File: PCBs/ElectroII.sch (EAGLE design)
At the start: 13 parts, among them U1 RFM95W-868S2

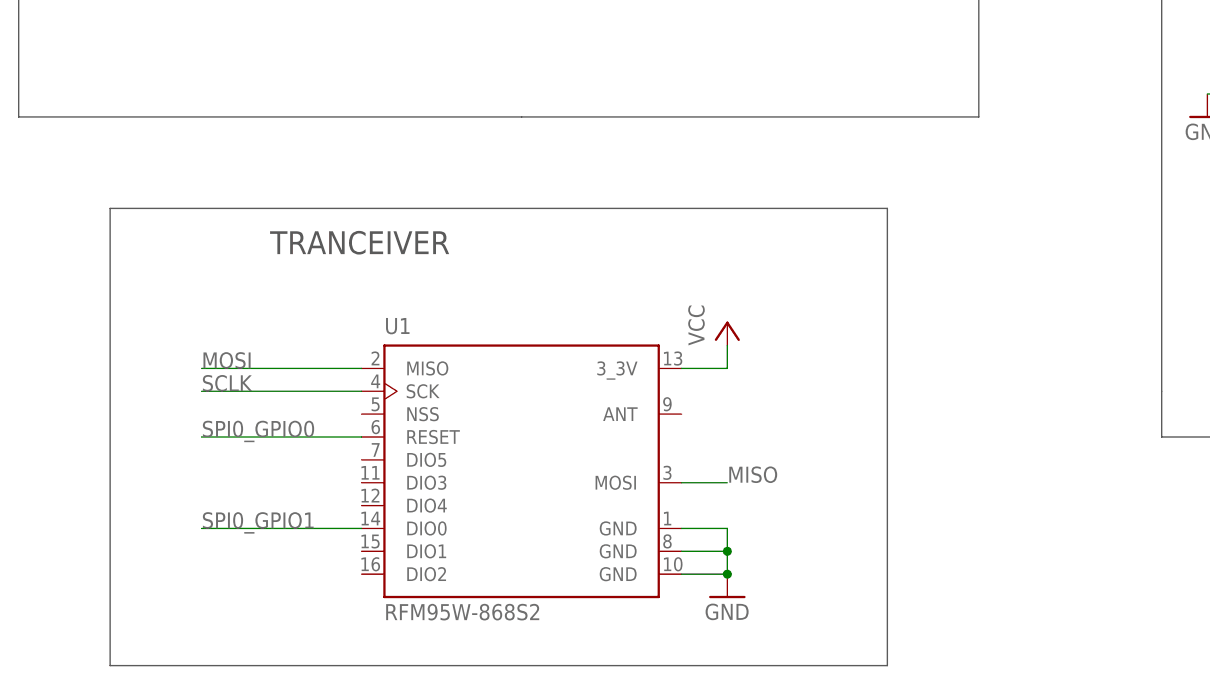
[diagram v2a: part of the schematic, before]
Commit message: Laid out rough PCB for Electro II
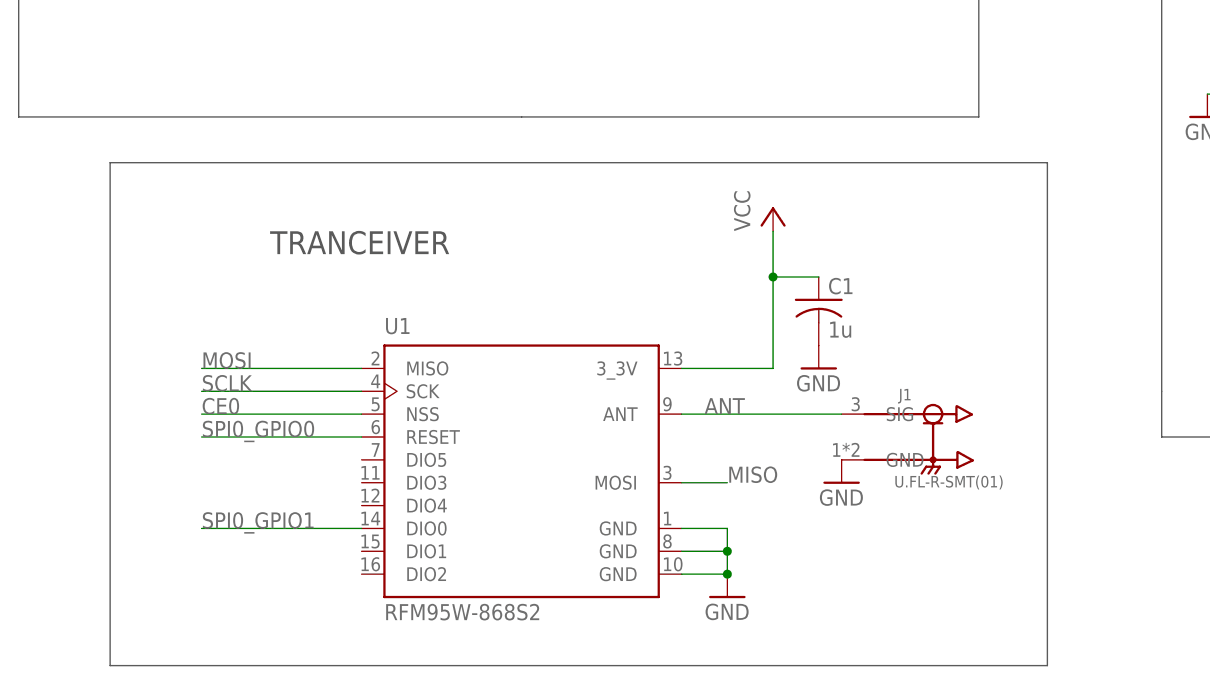
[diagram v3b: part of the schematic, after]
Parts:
- added C1: 1u, RTR Main Library:C-ALL_PACKAGESC1206
- added J1: U.FL-R-SMT(01), RTR Main Library:U.FL-R-SMT(01)
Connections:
- new net ANT: J1.SIG, U1.ANT
- net CE0: now also U1.NSS
- net GND: now also C1.2, J1.GND
- net VCC: now also C1.1
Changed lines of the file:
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@@
 <class number="0" name="default" width="0" drill="0">
+</class>
+<class number="1" name="PWR" width="0.6096" drill="0">
+<clearance class="1" value="0.508"/>
+</class>
+<class number="2" name="GND" width="0.762" drill="0">
+<clearance class="2" value="0.508"/>
 </class>
 </classes>
@@
 <part name="P+8" library="RTR Main Library" deviceset="VCC" device=""/>
 <part name="GND14" library="RTR Main Library" deviceset="GND" device=""/>
+<part name="J1" library="RTR Main Library" deviceset="U.FL-R-SMT(01)" device=""/>
+<part name="GND15" library="RTR Main Library" deviceset="GND" device=""/>
+<part name="C1" library="RTR Main Library" deviceset="C-ALL_PACKAGES" device="C1206" value="1u"/>
+<part name="GND16" library="RTR Main Library" deviceset="GND" device=""/>
 </parts>
 <sheets>
@@
 <wire x1="73.66" y1="-104.14" x2="154.94" y2="-104.14" width="0.1524" layer="97"/>
 <wire x1="154.94" y1="-104.14" x2="177.8" y2="-104.14" width="0.1524" layer="97"/>
-<wire x1="-43.18" y1="-78.74" x2="-43.18" y2="-129.54" width="0.1524" layer="97"/>
-<wire x1="-43.18" y1="-129.54" x2="43.18" y2="-129.54" width="0.1524" layer="97"/>
-<wire x1="43.18" y1="-129.54" x2="43.18" y2="-78.74" width="0.1524" layer="97"/>
-<wire x1="43.18" y1="-78.74" x2="-43.18" y2="-78.74" width="0.1524" layer="97"/>
+<wire x1="-43.18" y1="-73.66" x2="-43.18" y2="-129.54" width="0.1524" layer="97"/>
+<wire x1="-43.18" y1="-129.54" x2="60.96" y2="-129.54" width="0.1524" layer="97"/>
+<wire x1="60.96" y1="-129.54" x2="60.96" y2="-73.66" width="0.1524" layer="97"/>
+<wire x1="60.96" y1="-73.66" x2="-43.18" y2="-73.66" width="0.1524" layer="97"/>
 <text x="-25.4" y="-83.82" size="2.54" layer="97">TRANCEIVER</text>
 </plain>
@@
 <attribute name="VALUE" x="22.86" y="-124.46" size="1.778" layer="96"/>
 </instance>
-<instance part="P+8" gate="VCC" x="25.4" y="-91.44" smashed="yes">
-<attribute name="VALUE" x="22.86" y="-93.98" size="1.778" layer="96" rot="R90"/>
+<instance part="P+8" gate="VCC" x="30.48" y="-78.74" smashed="yes">
+<attribute name="VALUE" x="27.94" y="-81.28" size="1.778" layer="96" rot="R90"/>
 </instance>
 <instance part="GND14" gate="1" x="-45.72" y="-20.32" smashed="yes">
 <attribute name="VALUE" x="-48.26" y="-22.86" size="1.778" layer="96"/>
+</instance>
+<instance part="J1" gate="G$1" x="48.26" y="-104.14" smashed="yes">
+<attribute name="NAME" x="44.44143125" y="-100.06686875" size="1.27285" layer="95"/>
+<attribute name="VALUE" x="43.93218125" y="-109.7407" size="1.27288125" layer="96"/>
+</instance>
+<instance part="GND15" gate="1" x="38.1" y="-109.22" smashed="yes">
+<attribute name="VALUE" x="35.56" y="-111.76" size="1.778" layer="96"/>
+</instance>
+<instance part="C1" gate="G$1" x="35.56" y="-88.9" smashed="yes">
+<attribute name="NAME" x="36.576" y="-88.265" size="1.778" layer="95"/>
+<attribute name="VALUE" x="36.576" y="-93.091" size="1.778" layer="96"/>
+</instance>
+<instance part="GND16" gate="1" x="35.56" y="-96.52" smashed="yes">
+<attribute name="VALUE" x="33.02" y="-99.06" size="1.778" layer="96"/>
 </instance>
 </instances>
@@
 </busses>
 <nets>
-<net name="5V" class="0">
+<net name="5V" class="1">
 <segment>
 <pinref part="U$1" gate="G$1" pin="5V0@1"/>
@@
 <wire x1="88.9" y1="30.48" x2="81.28" y2="30.48" width="0.1524" layer="91"/>
 <label x="81.28" y="30.48" size="1.778" layer="95"/>
+</segment>
+<segment>
+<pinref part="U1" gate="G$1" pin="NSS"/>
+<wire x1="-15.24" y1="-101.6" x2="-33.02" y2="-101.6" width="0.1524" layer="91"/>
+<label x="-33.02" y="-101.6" size="1.778" layer="95"/>
 </segment>
 </net>
@@
 </segment>
 </net>
-<net name="GND" class="0">
+<net name="GND" class="2">
 <segment>
 <pinref part="SPI0" gate="G$1" pin="11"/>
@@
 <pinref part="U$1" gate="G$1" pin="GND@3"/>
 </segment>
+<segment>
+<pinref part="J1" gate="G$1" pin="GND"/>
+<pinref part="GND15" gate="1" pin="GND"/>
+</segment>
+<segment>
+<pinref part="C1" gate="G$1" pin="2"/>
+<pinref part="GND16" gate="1" pin="GND"/>
+</segment>
 </net>
 <net name="MOSI" class="0">
@@
 </segment>
 </net>
-<net name="VCC" class="0">
+<net name="VCC" class="1">
 <segment>
 <pinref part="SPI0" gate="G$1" pin="1"/>
@@
 <segment>
 <pinref part="U1" gate="G$1" pin="3_3V"/>
-<wire x1="20.32" y1="-96.52" x2="25.4" y2="-96.52" width="0.1524" layer="91"/>
+<wire x1="20.32" y1="-96.52" x2="30.48" y2="-96.52" width="0.1524" layer="91"/>
 <pinref part="P+8" gate="VCC" pin="VCC"/>
-<wire x1="25.4" y1="-96.52" x2="25.4" y2="-93.98" width="0.1524" layer="91"/>
+<wire x1="30.48" y1="-96.52" x2="30.48" y2="-86.36" width="0.1524" layer="91"/>
+<pinref part="C1" gate="G$1" pin="1"/>
+<wire x1="30.48" y1="-86.36" x2="30.48" y2="-81.28" width="0.1524" layer="91"/>
+<wire x1="35.56" y1="-86.36" x2="30.48" y2="-86.36" width="0.1524" layer="91"/>
+<junction x="30.48" y="-86.36"/>
 </segment>
 </net>
@@
 </segment>
 </net>
+<net name="ANT" class="0">
+<segment>
+<pinref part="U1" gate="G$1" pin="ANT"/>
+<pinref part="J1" gate="G$1" pin="SIG"/>
+<wire x1="20.32" y1="-101.6" x2="38.1" y2="-101.6" width="0.1524" layer="91"/>
+<label x="22.86" y="-101.6" size="1.778" layer="95"/>
+</segment>
+</net>

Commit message: Lots of progress on boost converter
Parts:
- added C2: 100u, RTR Main Library:C-ALL_PACKAGESC1206
- added C3: 10u, RTR Main Library:C-ALL_PACKAGESC1206
- added CN1: (no value), adafruit:JST_2PIN-SMT-RA
- added D1: 1N4004, adafruit:1N4004
- added L1: 6.8u, RTR Main Library:L_SMD
- added LOBAT: RED, RTR Main Library:LED5MM
- added PWR: GRN, RTR Main Library:LED5MM
- added R1: 1.85M, RTR Main Library:R-ALL_PACKAGESR1206
- added R2, R4: 200k, RTR Main Library:R-ALL_PACKAGESR1206
- added R3: 1.1M, RTR Main Library:R-ALL_PACKAGESR1206
- added R5, R6: (no value), RTR Main Library:R-ALL_PACKAGESR1206
- added U2: TPS61090RSAR, TPS61090RSAR:TPS61090RSAR
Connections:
- new net FB: R1.1, R2.2, U2.FB
- new net LBI: R3.1, R4.2, U2.LBI
- new net N$1: LOBAT.A, R6.1
- new net N$2: LOBAT.C, U2.LBO
- new net N$4: L1.2, U2.SW
- new net N$5: PWR.C, R5.2
- new net VBAT: C3.1, D1.C, L1.1, R3.2, U2.EN, U2.VBAT
- net GND: now also C2.2, C3.2, CN1.1, D1.A, R2.1, R4.1, R5.1, U2.EXT_PAD, U2.GND, U2.PGND, U2.SYNC
- net VCC: now also C2.1, PWR.A, R1.2, R6.2, U2.VOUT
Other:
- note added: "BOOST CONVERTER"

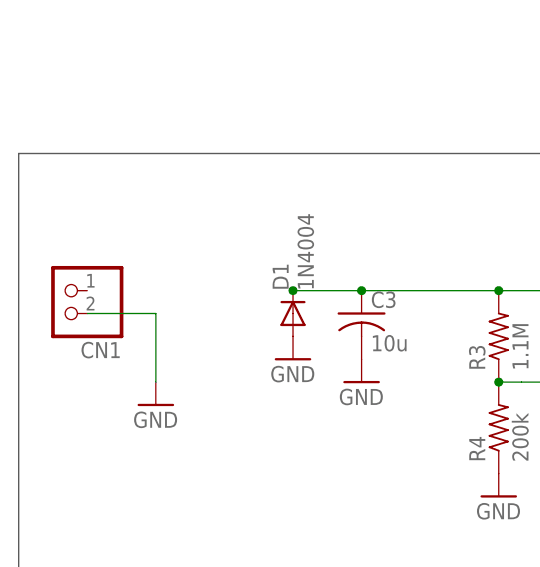
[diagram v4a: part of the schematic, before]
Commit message: More details on boost converter
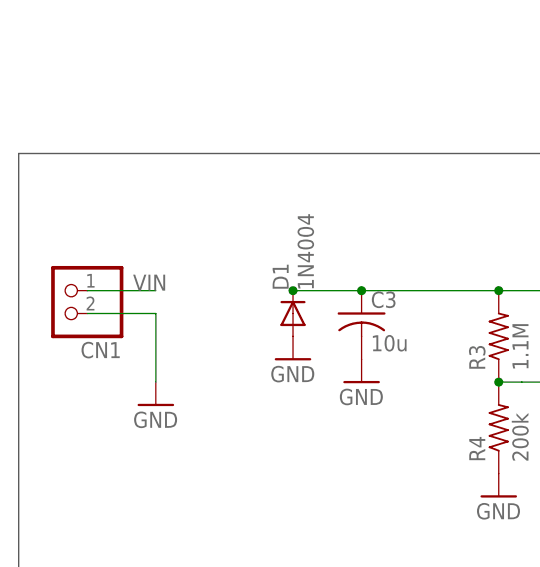
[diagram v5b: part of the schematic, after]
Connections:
- new net VIN: CN1.2
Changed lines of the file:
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@@
 <class number="0" name="default" width="0" drill="0">
 </class>
-<class number="1" name="PWR" width="0.6096" drill="0">
-<clearance class="1" value="0.1778"/>
+<class number="1" name="PWR" width="0.508" drill="0">
+<clearance class="1" value="0.1524"/>
 </class>
-<class number="2" name="GND" width="0.762" drill="0">
-<clearance class="2" value="0.1778"/>
+<class number="2" name="GND" width="0.508" drill="0">
+<clearance class="2" value="0.1524"/>
 </class>
 </classes>
@@
 </segment>
 </net>
-<net name="VBAT" class="0">
+<net name="VBAT" class="1">
 <segment>
 <pinref part="U2" gate="G$1" pin="VBAT"/>
@@
 </segment>
 </net>
+<net name="VIN" class="1">
+<segment>
+<pinref part="CN1" gate="G$1" pin="2"/>
+<wire x1="-254" y1="-22.86" x2="-246.38" y2="-22.86" width="0.1524" layer="91"/>
+<label x="-248.92" y="-22.86" size="1.778" layer="95"/>
+</segment>
+</net>

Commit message: Concept trace layouts
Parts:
- added F1: NANOSMDC110F-2, NANOSMDC110F-2:NANOSMDC110F-2
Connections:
- net 5V: now also C2.1, PWR.A, R1.2, R6.2, U2.VOUT
- net VBAT: now also F1.2
- net VCC: no longer C2.1, PWR.A, R1.2, R6.2, U2.VOUT
- net VIN: now also F1.1
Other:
- moved on the sheet: CN1, D1
